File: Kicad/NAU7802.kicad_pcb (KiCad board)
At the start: 2 copper layers, 25.8 x 33.5 mm, 20 parts, among them J2 B scale, J3 I²C, J4 Scale, J5 AVDD, J6 INT, U1 NAU7802SGI

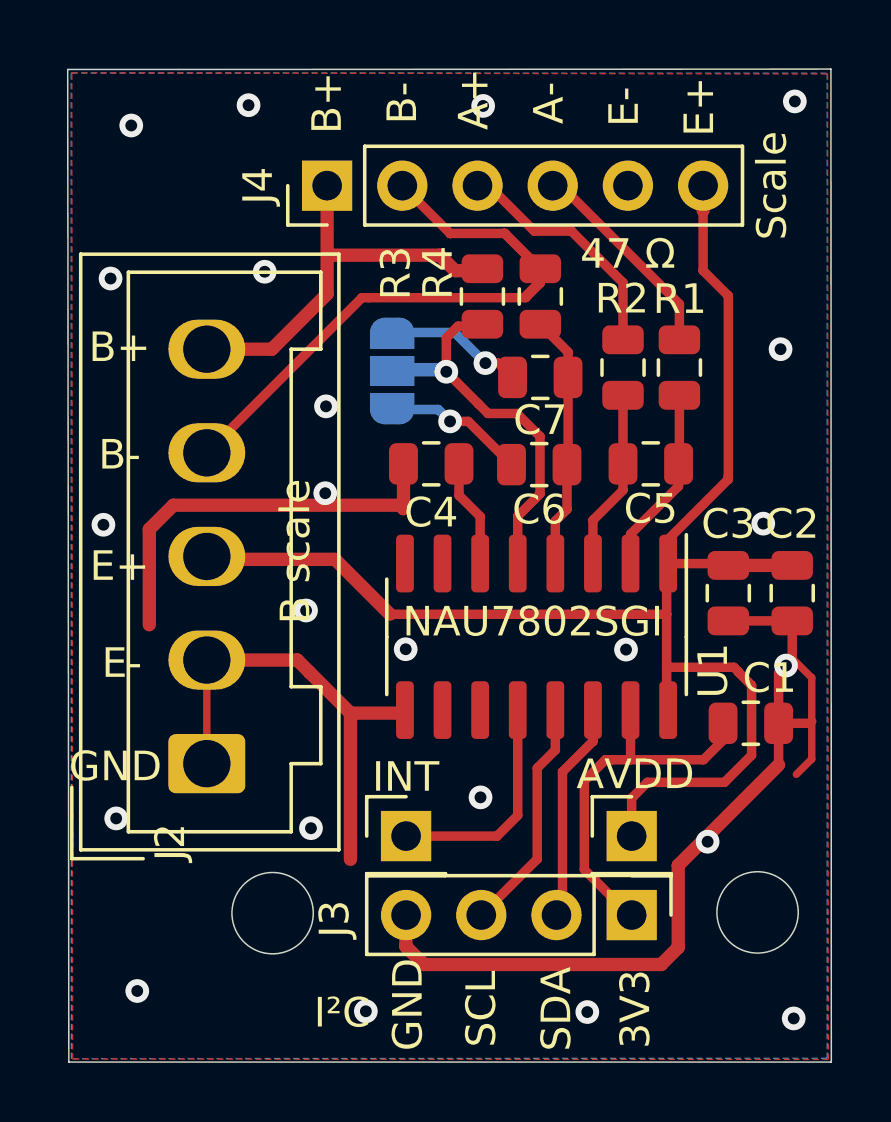
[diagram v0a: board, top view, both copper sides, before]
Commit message: ADD I²C Pullup + Jumper
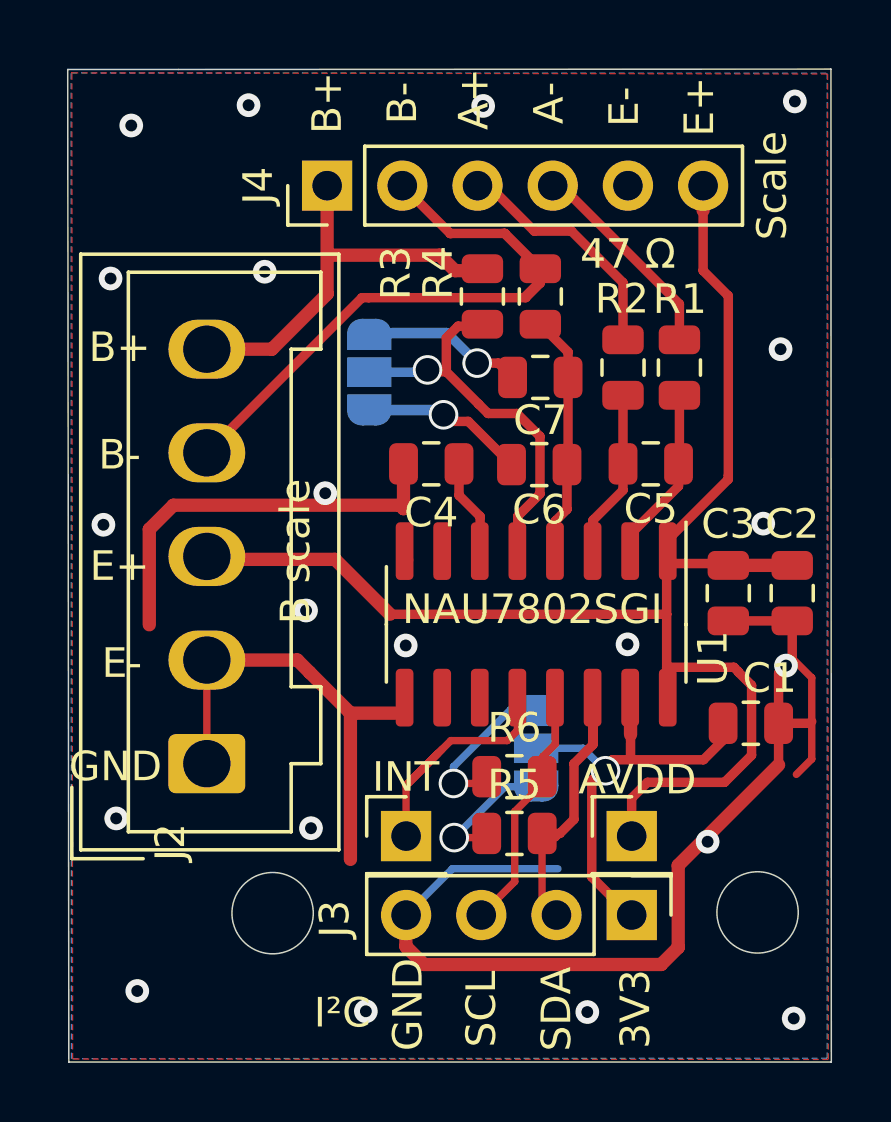
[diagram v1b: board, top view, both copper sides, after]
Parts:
- added I2C Pullup: Jumper_NC_Dual, Jumper:SolderJumper-3_P1.3mm_Open_RoundedPad1.0x1.5mm, B.Cu at (46.6, 50.9)
- added R5: R, Resistor_SMD:R_0805_2012Metric, F.Cu at (45.8, 53.8)
- added R6: R, Resistor_SMD:R_0805_2012Metric, F.Cu at (45.8, 51.8)
- JP1: renamed from B-Chanel; value en -> B-enabled
- moved JP1 0.78 mm to (40.9, 38.2)
- moved U1 0.42 mm to (46.6, 46.7)
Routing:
- net AVSS: track 65.8 -> 71.6 mm, vias 23 -> 21
- net Net-(JP2-Pad1): track 0.00 -> 5.34 mm, vias 0 -> 1
- net SCL: track 14.6 -> 9.41 mm
- net SDA: track 8.16 -> 13.0 mm
- net Net-(JP2-Pad3): track 0.00 -> 4.57 mm, vias 0 -> 1
- net Net-(C7-Pad1): track 4.69 -> 8.75 mm
- net INT: track 7.62 -> 11.4 mm
- net Net-(C6-Pad1): track 5.65 -> 8.22 mm
- net DVDD: track 15.4 -> 17.8 mm, vias 0 -> 1
- net Net-(JP1-Pad2): track 14.3 -> 13.9 mm, vias 1 -> 2

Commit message: add v1.4
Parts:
- moved JP1 0.72 mm to (40.2, 38.2)
- moved R3 0.70 mm to (44.1, 35.4)
- moved R4 0.57 mm to (46.2, 35.4)
- moved R2 0.26 mm to (51.7, 38.0)
- moved R6 0.12 mm to (45.9, 51.7)
- moved R5 0.10 mm to (45.9, 53.7)
- moved C7 0.09 mm to (46.7, 38.3)
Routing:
- net AVSS: track 71.6 -> 146.4 mm
- net B-: track 32.4 -> 20.2 mm
- net AVDD: track 52.6 -> 56.6 mm
- net INT: track 11.4 -> 7.93 mm
- net DVDD: track 17.8 -> 20.1 mm
- net Net-(JP1-Pad2): track 13.9 -> 15.6 mm, vias 2 -> 1
- net Net-(C6-Pad2): track 8.65 -> 10.3 mm
- net Net-(JP2-Pad1): track 5.34 -> 6.69 mm
- net Net-(JP2-Pad3): track 4.57 -> 5.91 mm
- net B+: track 16.7 -> 15.8 mm
- net SDA: track 13.0 -> 12.3 mm
- net Net-(C6-Pad1): track 8.22 -> 7.62 mm
- net Net-(C7-Pad1): track 8.75 -> 9.30 mm
